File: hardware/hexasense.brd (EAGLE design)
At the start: 100 x 62 mm, 41 parts

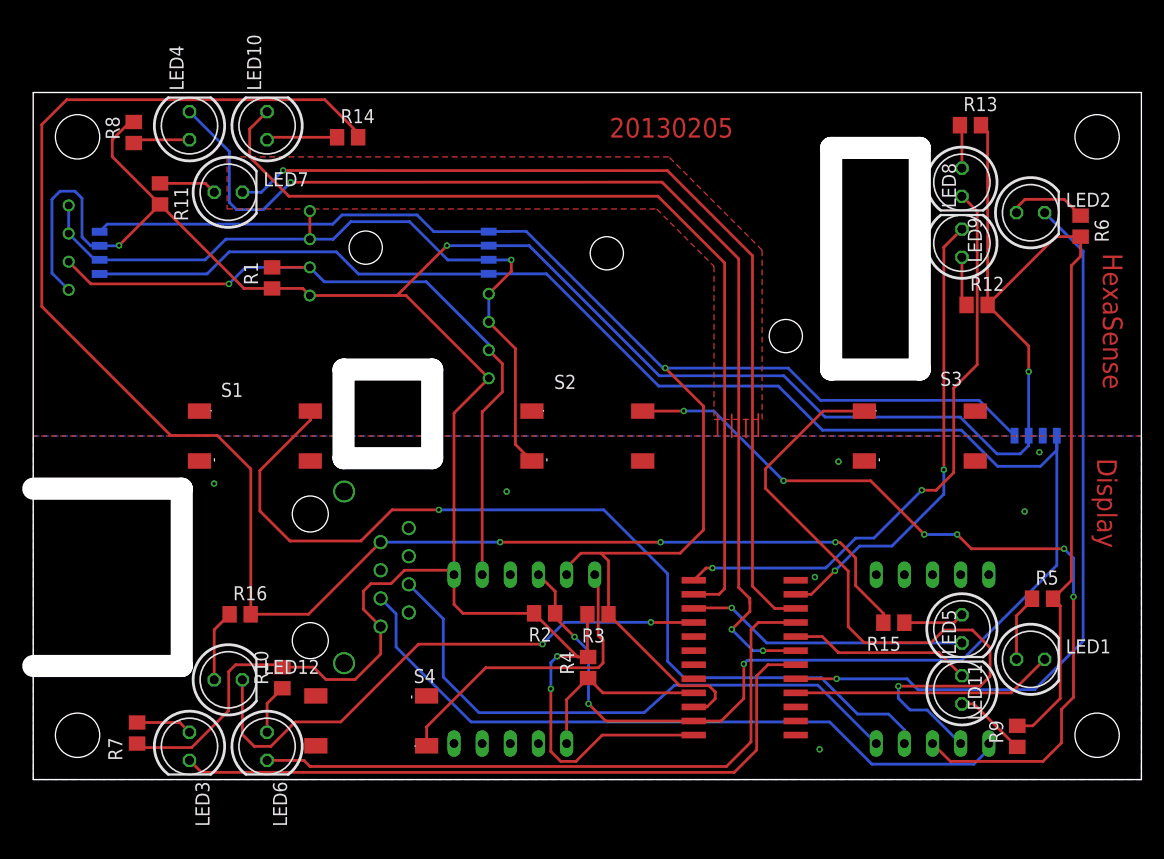
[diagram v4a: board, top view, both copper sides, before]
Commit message: added 100nF capacitors to humidity sensor and LED chip
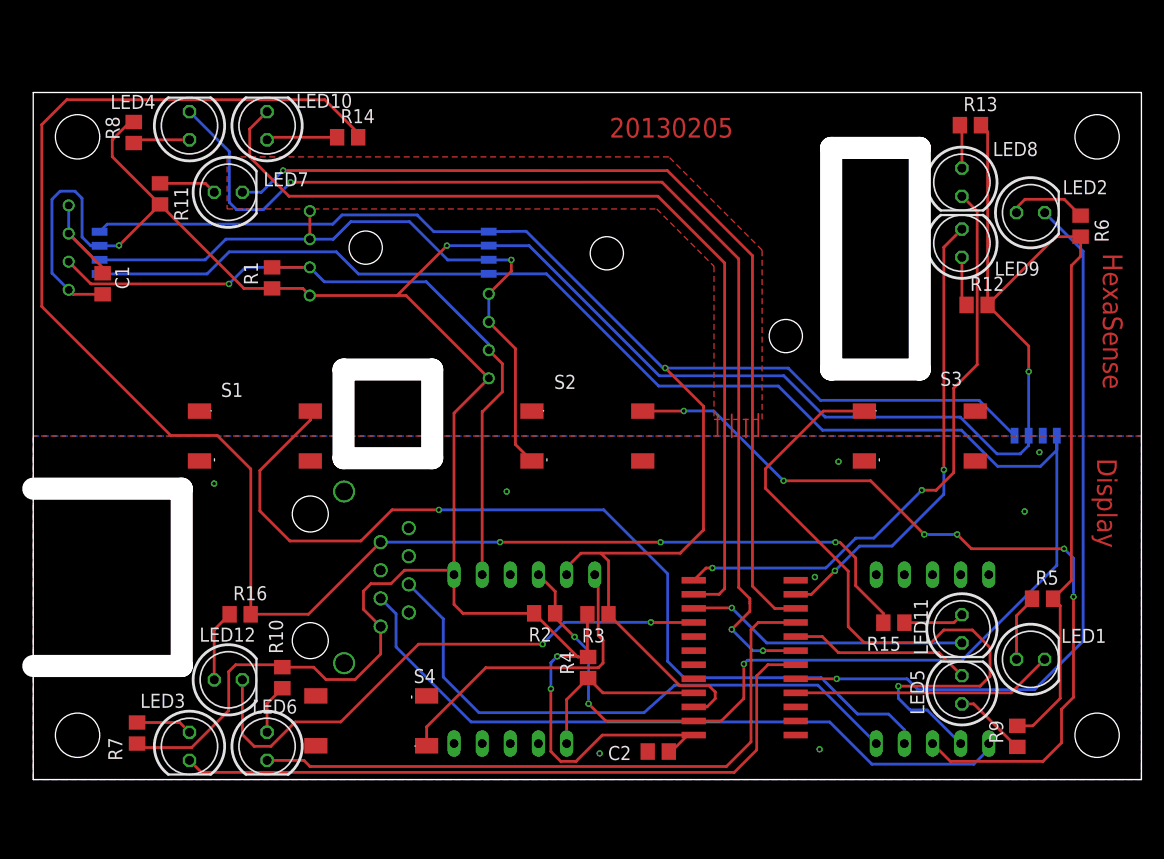
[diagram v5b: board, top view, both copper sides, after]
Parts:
- added C1, C2: 100n, rcl:C0805
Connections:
- net +3V3: now also C1.1, C2.1
- net GND: now also C1.2, C2.2
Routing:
- net +3V3: track 336.0 -> 341.6 mm
- net GND: track 77.1 -> 81.9 mm, vias 8 -> 9
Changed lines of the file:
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@@
 </autorouter>
 <elements>
-<element name="LED1" library="led" package="LED5MM" value="RED" x="90" y="10.85"/>
-<element name="LED4" library="led" package="LED5MM" value="RED" x="14.1" y="59" rot="R90"/>
-<element name="LED7" library="led" package="LED5MM" value="GREEN" x="17.6" y="53"/>
+<element name="LED1" library="led" package="LED5MM" value="RED" x="90" y="10.85" smashed="yes">
+<attribute name="NAME" x="92.755" y="12.3334" size="1.27" layer="25" ratio="10"/>
+</element>
+<element name="LED4" library="led" package="LED5MM" value="RED" x="14.1" y="59" smashed="yes" rot="R90">
+<attribute name="NAME" x="6.965" y="60.5134" size="1.27" layer="25" ratio="10"/>
+</element>
+<element name="LED7" library="led" package="LED5MM" value="GREEN" x="17.6" y="53" smashed="yes">
+<attribute name="NAME" x="20.775" y="53.5334" size="1.27" layer="25" ratio="10"/>
+</element>
 <element name="U$1" library="Reichelt" package="RJ45-REICHELT" value="MEBP8-8G" x="25" y="18.25" rot="MR90"/>
 <element name="U$2" library="humidity" package="HUMIDITY-SENSOR" value="HUMIDITY-SENSOR" x="38.96" y="47.49" rot="MR90"/>
@@
 <attribute name="NAME" x="20.28" y="44.635" size="1.27" layer="25" rot="R90"/>
 </element>
-<element name="LED2" library="led" package="LED5MM" value="RED" x="90" y="51.15"/>
-<element name="LED3" library="led" package="LED5MM" value="RED" x="14.1" y="3" rot="R270"/>
-<element name="LED5" library="led" package="LED5MM" value="GREEN" x="83.8" y="8.1" rot="R90"/>
-<element name="LED6" library="led" package="LED5MM" value="GREEN" x="21.1" y="3" rot="R270"/>
-<element name="LED8" library="led" package="LED5MM" value="GREEN" x="83.8" y="48.4" rot="R90"/>
-<element name="LED9" library="led" package="LED5MM" value="BLUE" x="83.8" y="53.9" rot="R270"/>
+<element name="LED2" library="led" package="LED5MM" value="RED" x="90" y="51.15" smashed="yes">
+<attribute name="NAME" x="92.885" y="52.8134" size="1.27" layer="25" ratio="10"/>
+</element>
+<element name="LED3" library="led" package="LED5MM" value="RED" x="14.1" y="3" smashed="yes" rot="R270">
+<attribute name="NAME" x="9.655" y="6.4734" size="1.27" layer="25" ratio="10"/>
+</element>
+<element name="LED5" library="led" package="LED5MM" value="GREEN" x="83.8" y="8.1" smashed="yes" rot="R90">
+<attribute name="NAME" x="80.4066" y="5.845" size="1.27" layer="25" ratio="10" rot="R90"/>
+</element>
+<element name="LED6" library="led" package="LED5MM" value="GREEN" x="21.1" y="3" smashed="yes" rot="R270">
+<attribute name="NAME" x="19.755" y="5.9534" size="1.27" layer="25" ratio="10"/>
+</element>
+<element name="LED8" library="led" package="LED5MM" value="GREEN" x="83.8" y="48.4" smashed="yes" rot="R90">
+<attribute name="NAME" x="86.595" y="56.2634" size="1.27" layer="25" ratio="10"/>
+</element>
+<element name="LED9" library="led" package="LED5MM" value="BLUE" x="83.8" y="53.9" smashed="yes" rot="R270">
+<attribute name="NAME" x="86.745" y="45.4734" size="1.27" layer="25" ratio="10"/>
+</element>
 <element name="U$3" library="philips" package="SO24" value="PCA9532D" x="64.2" y="11" smashed="yes" rot="R90"/>
 <element name="S1" library="Ergaenzung" package="TASTER-9314_SMD" value="" x="20" y="31" smashed="yes">
@@
 </element>
 <element name="R10" library="rcl" package="R0805" value="20R" x="22.48" y="9.19" smashed="yes" rot="R90">
-<attribute name="NAME" x="21.21" y="8.555" size="1.27" layer="25" rot="R90"/>
+<attribute name="NAME" x="22.54" y="11.355" size="1.27" layer="25" rot="R90"/>
 </element>
 <element name="R11" library="rcl" package="R0805" value="180R" x="11.44" y="52.85" smashed="yes" rot="R270">
@@
 <attribute name="NAME" x="83.935" y="60.32" size="1.27" layer="25"/>
 </element>
-<element name="R2" library="rcl" package="R0805" value="10k" x="46.15" y="15" rot="R180"/>
-<element name="R3" library="rcl" package="R0805" value="10k" x="50.96" y="14.91" rot="R180"/>
-<element name="R4" library="rcl" package="R0805" value="10k" x="50.07" y="10.11" rot="R90"/>
+<element name="R2" library="rcl" package="R0805" value="10k" x="46.15" y="15" smashed="yes" rot="R180">
+<attribute name="NAME" x="46.785" y="13.73" size="1.27" layer="25" rot="R180"/>
+</element>
+<element name="R3" library="rcl" package="R0805" value="10k" x="50.96" y="14.91" smashed="yes" rot="R180">
+<attribute name="NAME" x="51.595" y="13.64" size="1.27" layer="25" rot="R180"/>
+</element>
+<element name="R4" library="rcl" package="R0805" value="10k" x="50.07" y="10.11" smashed="yes" rot="R90">
+<attribute name="NAME" x="48.8" y="9.475" size="1.27" layer="25" rot="R90"/>
+</element>
 <element name="U$4" library="hexabus" package="HEXABUS" value="HEXABUS" x="64.2" y="17" rot="MR90"/>
 <element name="U$5" library="humidity" package="HUMIDITY-SENSOR" value="HUMIDITY-SENSOR" x="17.2" y="48" rot="MR90"/>
@@
 <element name="U$8" library="humidity" package="HYT271" value="HYT271" x="51.1" y="47.54" rot="MR90"/>
 <element name="U$9" library="humidity" package="HYT271" value="HYT271" x="90.46" y="41.03" rot="MR0"/>
-<element name="R14" library="rcl" package="R0805" value="180R" x="28.37" y="57.96"/>
-<element name="R15" library="rcl" package="R0805" value="180R" x="77.66" y="14.16" rot="R180"/>
-<element name="R16" library="rcl" package="R0805" value="180R" x="18.67" y="14.91"/>
-<element name="LED10" library="led" package="LED5MM" value="BLUE" x="21.1" y="59" rot="R90"/>
-<element name="LED11" library="led" package="LED5MM" value="BLUE" x="83.8" y="13.6" rot="R270"/>
-<element name="LED12" library="led" package="LED5MM" value="BLUE" x="17.6" y="9"/>
+<element name="R14" library="rcl" package="R0805" value="180R" x="28.37" y="57.96" smashed="yes">
+<attribute name="NAME" x="27.735" y="59.23" size="1.27" layer="25"/>
+</element>
+<element name="R15" library="rcl" package="R0805" value="180R" x="77.66" y="14.16" smashed="yes" rot="R180">
+<attribute name="NAME" x="78.295" y="12.89" size="1.27" layer="25" rot="R180"/>
+</element>
+<element name="R16" library="rcl" package="R0805" value="180R" x="18.67" y="14.91" smashed="yes">
+<attribute name="NAME" x="18.035" y="16.18" size="1.27" layer="25"/>
+</element>
+<element name="LED10" library="led" package="LED5MM" value="BLUE" x="21.1" y="59" smashed="yes" rot="R90">
+<attribute name="NAME" x="23.715" y="60.6134" size="1.27" layer="25" ratio="10"/>
+</element>
+<element name="LED11" library="led" package="LED5MM" value="BLUE" x="83.8" y="13.6" smashed="yes" rot="R270">
+<attribute name="NAME" x="79.4634" y="16.325" size="1.27" layer="25" ratio="10" rot="R270"/>
+</element>
+<element name="LED12" library="led" package="LED5MM" value="BLUE" x="17.6" y="9" smashed="yes">
+<attribute name="NAME" x="14.995" y="12.4434" size="1.27" layer="25" ratio="10"/>
+</element>
+<element name="C1" library="rcl" package="C0805" value="100n" x="6.26" y="44.74" smashed="yes" rot="R90">
+<attribute name="NAME" x="7.39" y="46.34" size="1.27" layer="25" rot="R270"/>
+</element>
+<element name="C2" library="rcl" package="C0805" value="100n" x="56.4" y="2.53" smashed="yes" rot="R180">
+<attribute name="NAME" x="53.96" y="3.03" size="1.27" layer="25" rot="R180"/>
+</element>
 </elements>
 <signals>
@@
 <wire x1="43.14" y1="46.89" x2="43.14" y2="45.86" width="0.254" layer="1"/>
 <wire x1="43.14" y1="45.86" x2="41.11" y2="43.83" width="0.254" layer="1"/>
+<wire x1="3.2" y1="51.81" x2="3.2" y2="49.27" width="0.254" layer="16"/>
+<wire x1="5.99" y1="46.895" x2="5.575" y2="46.895" width="0.254" layer="16"/>
+<wire x1="5.575" y1="46.895" x2="3.2" y2="49.27" width="0.254" layer="16"/>
+<contactref element="C1" pad="2"/>
+<wire x1="6.26" y1="45.69" x2="6.26" y2="46.21" width="0.254" layer="1"/>
+<wire x1="6.26" y1="46.21" x2="3.2" y2="49.27" width="0.254" layer="1"/>
+<contactref element="C2" pad="2"/>
+<via x="51.11" y="2.36" extent="1-16" drill="0.3"/>
 <wire x1="64.31" y1="30.87" x2="65.43" y2="30.98" width="0" layer="19" extent="1-1"/>
 <wire x1="63.03" y1="30.88" x2="64.31" y2="30.87" width="0" layer="19" extent="1-1"/>
 <wire x1="61.75" y1="31.1" x2="63.03" y2="30.88" width="0" layer="19" extent="1-1"/>
-<wire x1="3.2" y1="51.81" x2="3.2" y2="49.27" width="0.254" layer="16"/>
-<wire x1="5.99" y1="46.895" x2="5.575" y2="46.895" width="0.254" layer="16"/>
-<wire x1="5.575" y1="46.895" x2="3.2" y2="49.27" width="0.254" layer="16"/>
 </signal>
 <signal name="+3V3">
@@
 <wire x1="33.5" y1="18.89" x2="37.57" y2="18.89" width="0.254" layer="1"/>
 <wire x1="37.57" y1="18.89" x2="37.97" y2="18.49" width="0.254" layer="1"/>
-<wire x1="24.96" y1="43.68" x2="32.74" y2="43.68" width="0.254" layer="1"/>
-<wire x1="32.74" y1="43.68" x2="32.83" y2="43.68" width="0.254" layer="1"/>
+<wire x1="24.96" y1="43.68" x2="32.83" y2="43.68" width="0.254" layer="1"/>
 <wire x1="32.83" y1="43.68" x2="37.33" y2="48.18" width="0.254" layer="1"/>
 <via x="37.33" y="48.18" extent="1-16" drill="0.3"/>
 <wire x1="37.33" y1="48.18" x2="41.095" y2="48.18" width="0.254" layer="16"/>
 <wire x1="41.095" y1="48.18" x2="41.1" y2="48.175" width="0.254" layer="16"/>
-<wire x1="59.6" y1="4.015" x2="51.345" y2="4.015" width="0.254" layer="1"/>
+<wire x1="59.6" y1="4.015" x2="59.07" y2="4.015" width="0.254" layer="1"/>
+<wire x1="59.07" y1="4.015" x2="51.345" y2="4.015" width="0.254" layer="1"/>
 <wire x1="51.345" y1="4.015" x2="48.97" y2="1.64" width="0.254" layer="1"/>
 <wire x1="48.97" y1="1.64" x2="47.6" y2="1.64" width="0.254" layer="1"/>
@@
 <wire x1="41.11" y1="36.21" x2="33.64" y2="43.68" width="0.254" layer="1"/>
 <wire x1="33.64" y1="43.68" x2="32.83" y2="43.68" width="0.254" layer="1"/>
+<contactref element="C1" pad="1"/>
+<wire x1="6.26" y1="43.79" x2="3.6" y2="43.79" width="0.254" layer="1"/>
+<wire x1="3.6" y1="43.79" x2="3.2" y2="44.19" width="0.254" layer="1"/>
+<contactref element="C2" pad="1"/>
+<wire x1="57.35" y1="2.53" x2="57.585" y2="2.53" width="0.254" layer="1"/>
+<wire x1="57.585" y1="2.53" x2="59.07" y2="4.015" width="0.254" layer="1"/>
 </signal>
 <signal name="TEMP_1">
